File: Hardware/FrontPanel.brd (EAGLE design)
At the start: 100 x 61 mm, 30 parts, among them U1 TPIC6B595N, U2 TPIC6B595N, U3 TPIC6B595N, U4 TPIC6B595N, U5 TPIC6B595N, U6 TPIC6B595N

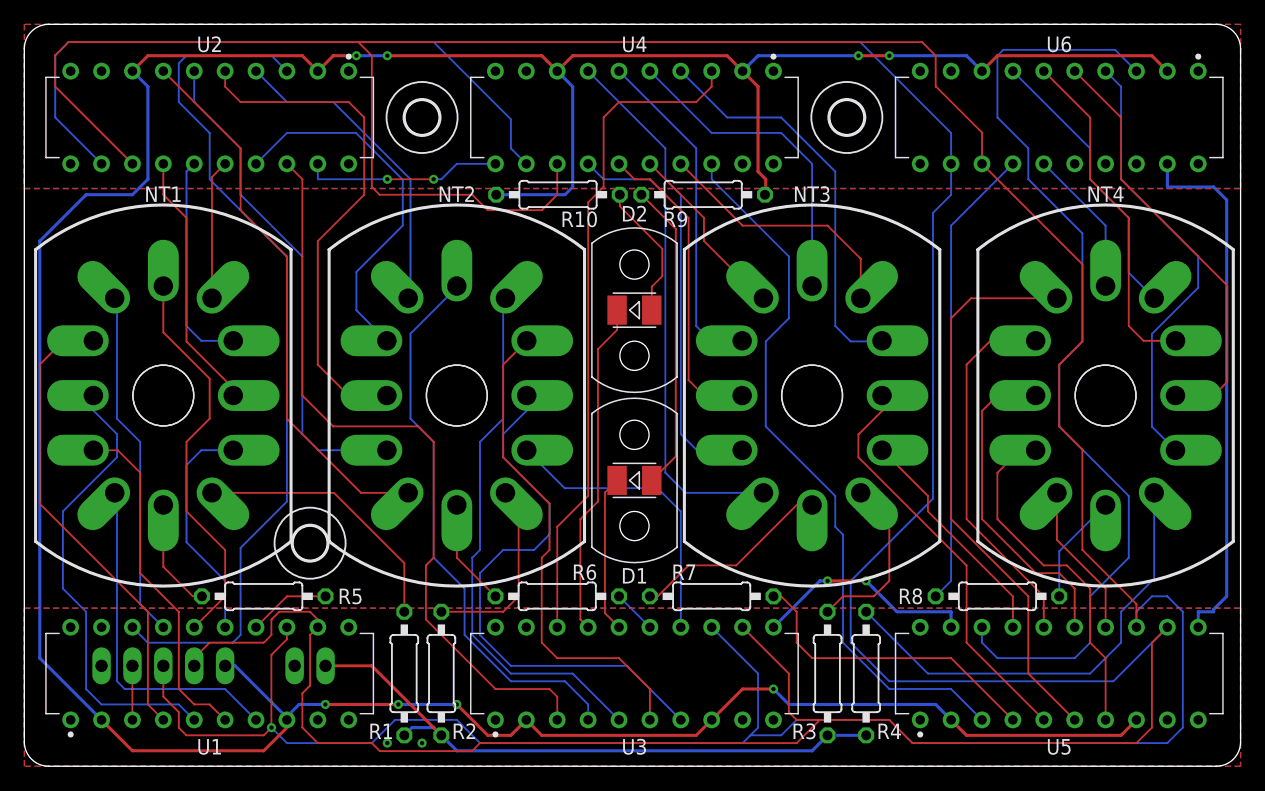
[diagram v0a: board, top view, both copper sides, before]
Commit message: fixed ERC errors
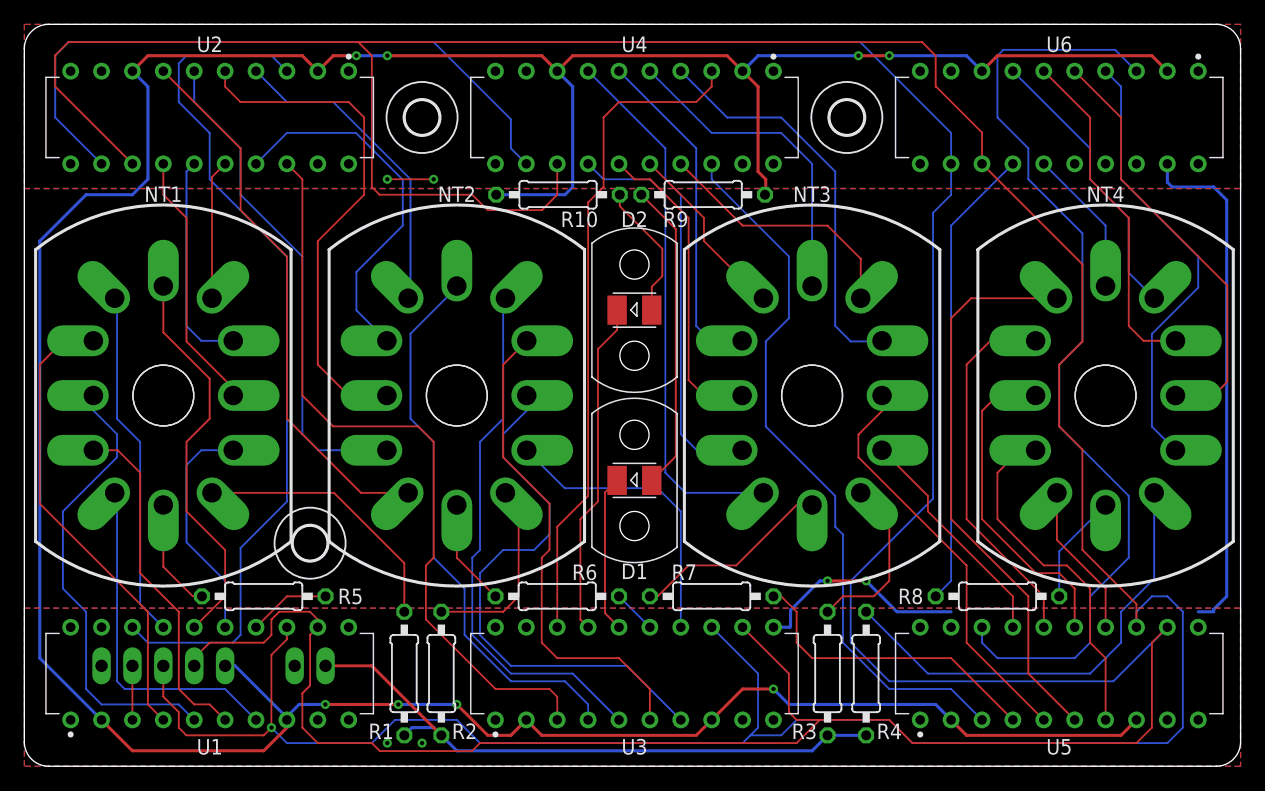
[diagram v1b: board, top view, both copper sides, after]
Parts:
- D1, D2: value (none) -> RED/AMBER; device Wurth_Elektronik_Optoelectronics_rev17b:WL-SMTW_3528 -> Wurth_Elektronik_Optoelectronics_rev18a:WL-SITW_154141XXBA210
- DATA, HV: value (none) -> .1" Header
- turned D1 to 180 degrees
- turned D2 to 180 degrees
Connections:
- net +160V renamed V+
- net +5V renamed VCC
- net LED1: now also D1.2; no longer D1.1
- net LED2: now also D2.2; no longer D2.1
- net N$66: now also D1.1; no longer D1.2
- net N$67: now also D2.1; no longer D2.2
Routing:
- net GND: track 79.0 -> 64.4 mm
